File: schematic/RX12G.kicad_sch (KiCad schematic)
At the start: 11 parts, among them J1 ICSP, U1 PIC32MK1024GPK064-I/PT, X1 24 MHz

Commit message: Complete schematic
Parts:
- C1, C2, C3, C4, C5, C6, C7: footprint (none) -> Capacitor_SMD:C_0402_1005Metric
- J1: footprint (none) -> Connector_PinHeader_2.54mm:PinHeader_1x05_P2.54mm_Vertical
- R1: value R -> 10k; footprint (none) -> Resistor_SMD:R_0603_1608Metric
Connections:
- net CH9_SBUS4: now reaches U1.1 (TCK/RPA7/PMD5/RA7)
- net LED_SAT3: now reaches U1.11 (AN10/RPA12/RA12)
- net SAT3_RX: now reaches U1.12 (AN9/RPA11/RA11)
- net LED_SAT1: now reaches U1.14 (OA2IN+/AN1/C2IN1+/RPA1/RA1)
- net SAT1_RX: now reaches U1.15 (PGD3/VREF-/OA2IN-/AN2/C2IN1-/RPB0/CTED2/RB0)
- net Bind_Button: now reaches U1.16 (PGC3/OA1OUT/VREF+/AN3/C1IN4-/C4IN2-/RPB1/CTED1/PMA6/RB1)
- net LED_A: now reaches U1.21 (OA3OUT/AN6/C3IN4-/C4IN1+/C4IN4-/RPC0/RC0)
- net LED_B: now reaches U1.22 (OA3IN-/AN7/C3IN1-/C4IN1-/RPC1/PMA7/RC1)
- net IMU_INT2: now reaches U1.29 (AN14/RPE14/PMA1/RE14)
- net CH10_SBUS3: now reaches U1.3 (RPB15/PMD7/RB15)
- net IMU_INT1: now reaches U1.30 (AN15/RPE15/PMA0/RE15)
- net IMU_SDA: now reaches U1.31 (TDI/CDAC3/AN26/RPA8/SDA2/PMA9/RA8)
- net IMU_SCL: now reaches U1.32 (RPB4/SCL2/PMA8/RB4)
- net D-: now reaches U1.36 (D1-)
- net D+: now reaches U1.37 (D1+)
- net CH11_SBUS2: now reaches U1.4 (AN19/CVD19/RPG6/PMA5/RG6)
- net LED_SAT2: now reaches U1.42 (RD8)
- net SAT2_RX: now reaches U1.43 (PGD2/RPB5/SDA3/USBID1/RB5)
- net CH1: now reaches U1.49 (TMS/OA5IN-/AN27/CVD27/LVDIN/C5IN1-/RPB9/RB9)
- net CH2: now reaches U1.50 (TRCLK/RPC6/RC6)
- net CH3: now reaches U1.52 (TRD1/RPC8/PMWR/RC8)
- net CH4: now reaches U1.53 (TRD2/RPD5/PMRD/RD5)
- net CH5: now reaches U1.54 (TRD3/RPD6/RD6)
- net CH6: now reaches U1.55 (RPC9/RC9)
- net CH12_SBUS1: now reaches U1.6 (AN17/RPG8/SDA1/PMA3/RG8)
- net CH7: now reaches U1.62 (RPB12/PMD2/RB12)
- net CH8: now reaches U1.63 (RPB13/CTPLS/PMD3/RB13)
- no-connect marks 0 -> 20
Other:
- moved on the sheet: C1, C2, C3, C4, C5, C6, J1, R1

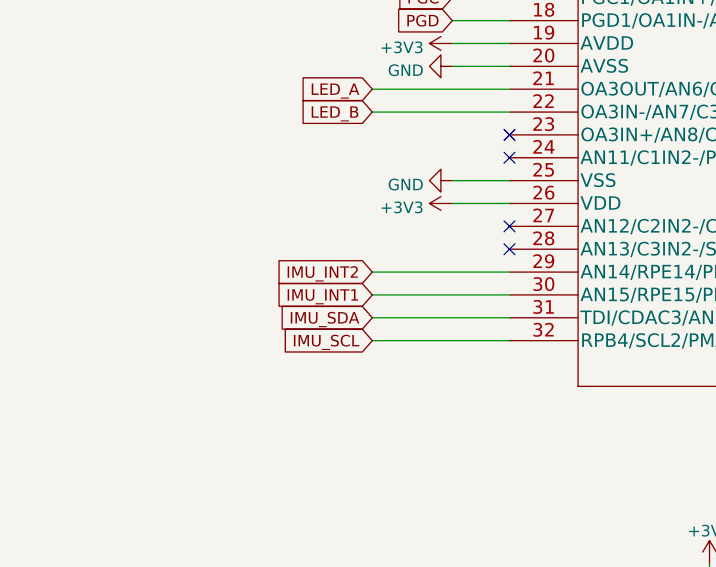
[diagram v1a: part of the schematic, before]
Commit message: Workable pcb layout
Needs work on silkscreen
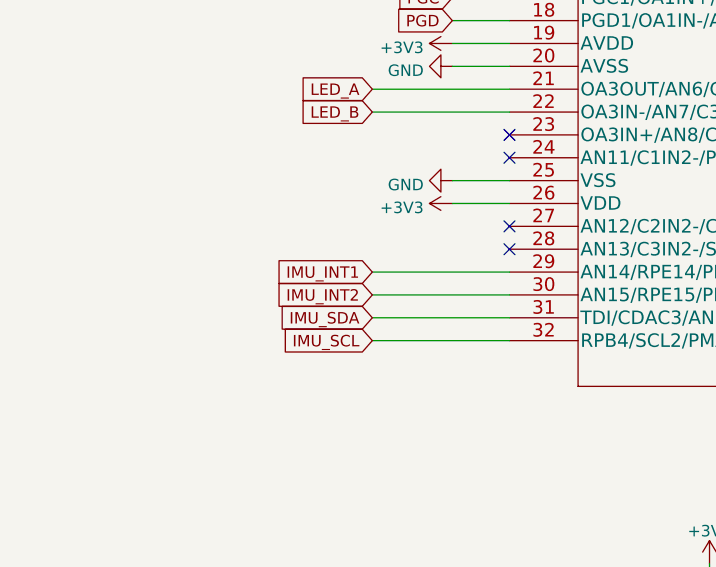
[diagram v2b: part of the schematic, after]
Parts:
- X1: footprint SamacSys Parts:AMPMAFB120000T -> SamacSys Parts:ASTMUPCE3312000MHZLJET
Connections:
- net IMU_INT1: now also U1.29 (AN14/RPE14/PMA1/RE14); no longer U1.30 (AN15/RPE15/PMA0/RE15)
- net IMU_INT2: now also U1.30 (AN15/RPE15/PMA0/RE15); no longer U1.29 (AN14/RPE14/PMA1/RE14)
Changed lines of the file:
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@@
+    (stroke (width 0) (type default) (color 0 0 0 0))
+  )
+  (wire (pts (xy 54.61 99.06) (xy 69.85 99.06))
     (stroke (width 0) (type default) (color 0 0 0 0))
   )
@@
     (stroke (width 0) (type default) (color 0 0 0 0))
   )
-  (wire (pts (xy 54.61 99.06) (xy 69.85 99.06))
-    (stroke (width 0) (type default) (color 0 0 0 0))
-  )
   (wire (pts (xy 92.075 131.445) (xy 92.075 135.255))
     (stroke (width 0) (type default) (color 0 0 0 0))
@@
     (stroke (width 0) (type default) (color 0 0 0 0))
   )
+  (wire (pts (xy 54.61 101.6) (xy 69.85 101.6))
+    (stroke (width 0) (type default) (color 0 0 0 0))
+  )
   (wire (pts (xy 130.175 142.875) (xy 142.875 142.875))
-    (stroke (width 0) (type default) (color 0 0 0 0))
-  )
-  (wire (pts (xy 54.61 101.6) (xy 69.85 101.6))
     (stroke (width 0) (type default) (color 0 0 0 0))
   )
@@
     )
   )
-  (global_label "IMU_INT1" (shape input) (at 54.61 101.6 180) (fields_autoplaced)
+  (global_label "IMU_INT1" (shape input) (at 54.61 99.06 180) (fields_autoplaced)
+    (effects (font (size 1.27 1.27)) (justify right))
+    (property "Intersheet References" "${INTERSHEET_REFS}" (id 0) (at 43.7302 98.9806 0)
+      (effects (font (size 1.27 1.27)) (justify right) hide)
+    )
+  )
+  (global_label "LED_A" (shape input) (at 54.61 78.74 180) (fields_autoplaced)
+    (effects (font (size 1.27 1.27)) (justify right))
+    (property "Intersheet References" "${INTERSHEET_REFS}" (id 0) (at 46.6936 78.6606 0)
+      (effects (font (size 1.27 1.27)) (justify right) hide)
+    )
+  )
+  (global_label "IMU_SCL" (shape input) (at 54.61 106.68 180) (fields_autoplaced)
+    (effects (font (size 1.27 1.27)) (justify right))
+    (property "Intersheet References" "${INTERSHEET_REFS}" (id 0) (at 44.335 106.6006 0)
+      (effects (font (size 1.27 1.27)) (justify right) hide)
+    )
+  )
+  (global_label "IMU_INT2" (shape input) (at 54.61 101.6 180) (fields_autoplaced)
     (effects (font (size 1.27 1.27)) (justify right))
     (property "Intersheet References" "${INTERSHEET_REFS}" (id 0) (at 43.7302 101.5206 0)
-      (effects (font (size 1.27 1.27)) (justify right) hide)
-    )
-  )
-  (global_label "LED_A" (shape input) (at 54.61 78.74 180) (fields_autoplaced)
-    (effects (font (size 1.27 1.27)) (justify right))
-    (property "Intersheet References" "${INTERSHEET_REFS}" (id 0) (at 46.6936 78.6606 0)
-      (effects (font (size 1.27 1.27)) (justify right) hide)
-    )
-  )
-  (global_label "IMU_SCL" (shape input) (at 54.61 106.68 180) (fields_autoplaced)
-    (effects (font (size 1.27 1.27)) (justify right))
-    (property "Intersheet References" "${INTERSHEET_REFS}" (id 0) (at 44.335 106.6006 0)
-      (effects (font (size 1.27 1.27)) (justify right) hide)
-    )
-  )
-  (global_label "IMU_INT2" (shape input) (at 54.61 99.06 180) (fields_autoplaced)
-    (effects (font (size 1.27 1.27)) (justify right))
-    (property "Intersheet References" "${INTERSHEET_REFS}" (id 0) (at 43.7302 98.9806 0)
       (effects (font (size 1.27 1.27)) (justify right) hide)
     )
@@
     (property "Reference" "X1" (id 0) (at 200.66 133.2443 0))
     (property "Value" "24 MHz" (id 1) (at 200.66 136.0194 0))
-    (property "Footprint" "SamacSys Parts:AMPMAFB120000T" (id 2) (at 212.09 137.16 0)
+    (property "Footprint" "SamacSys Parts:ASTMUPCE3312000MHZLJET" (id 2) (at 212.09 137.16 0)
       (effects (font (size 1.27 1.27)) (justify left) hide)
     )
@@
     )
     (path "/fb9fbb52-14d4-4062-9475-ec74defe9327"
-      (reference "X1") (unit 1) (value "24 MHz") (footprint "SamacSys Parts:AMPMAFB120000T")
-    )
-  )
+      (reference "X1") (unit 1) (value "24 MHz") (footprint "SamacSys Parts:ASTMUPCE3312000MHZLJET")
+    )
+  )

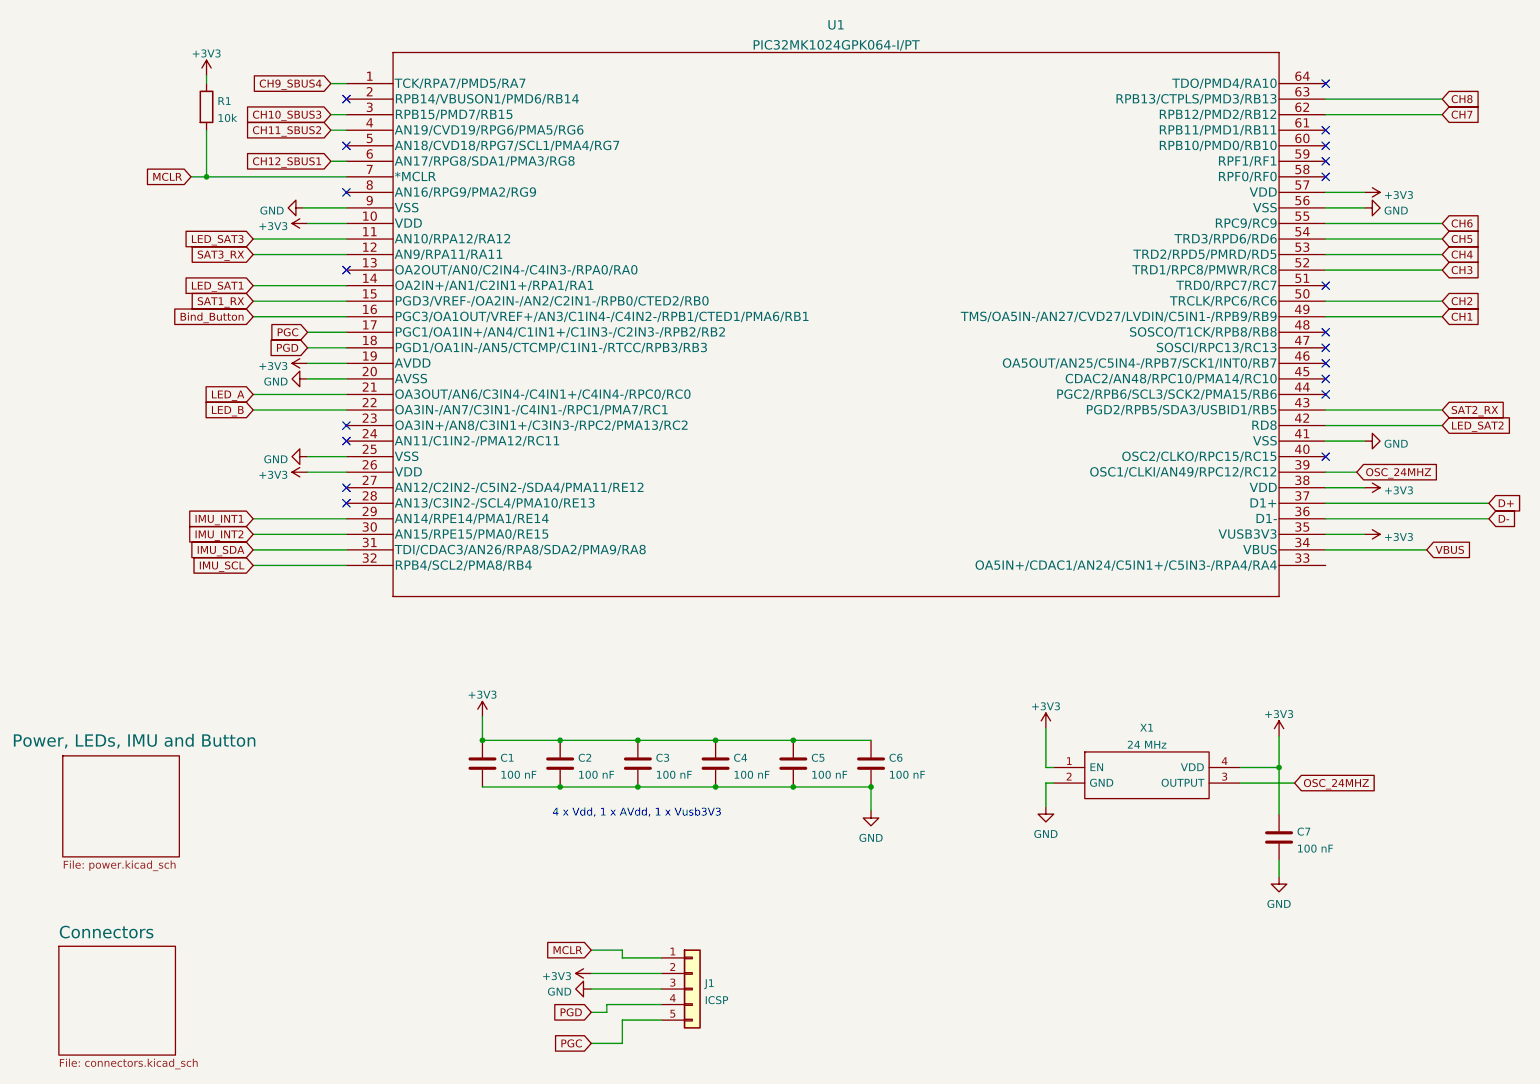
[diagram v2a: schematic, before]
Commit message: Fixed missing  SAT_POWER connection
Also re-assigned some pins to improve pcb layout
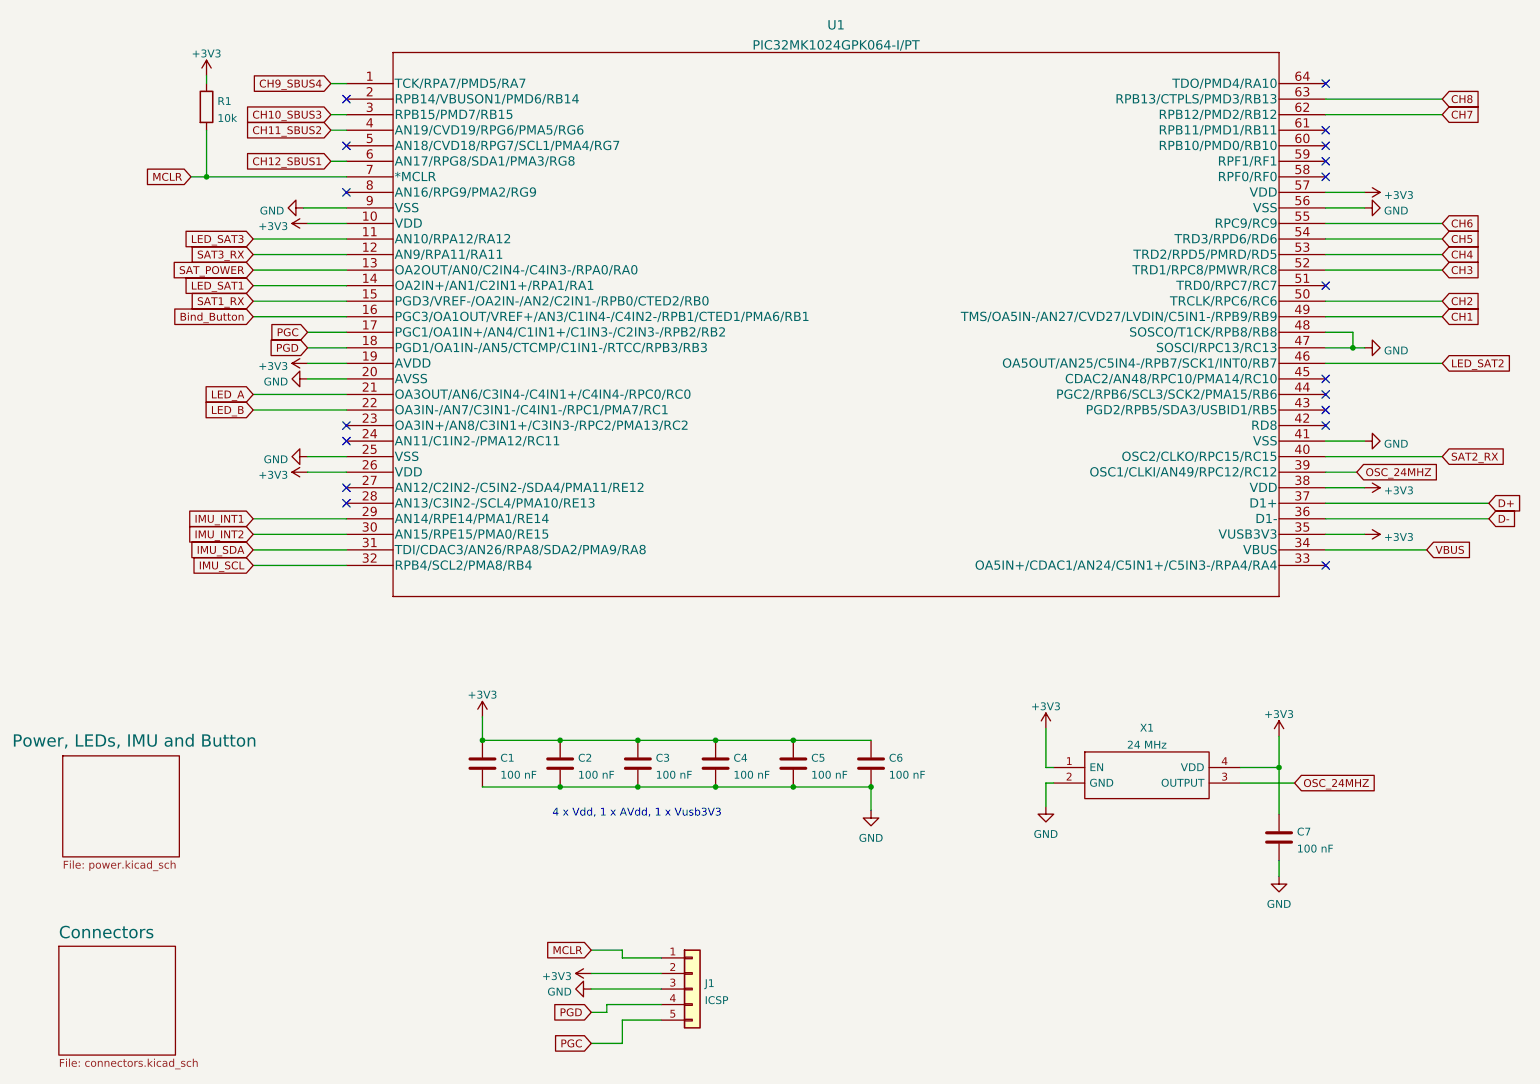
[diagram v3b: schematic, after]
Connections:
- net GND: now also U1.47 (SOSCI/RPC13/RC13), U1.48 (SOSCO/T1CK/RPB8/RB8)
- net LED_SAT2: now also U1.46 (OA5OUT/AN25/C5IN4-/RPB7/SCK1/INT0/RB7); no longer U1.42 (RD8)
- net SAT2_RX: now also U1.40 (OSC2/CLKO/RPC15/RC15); no longer U1.43 (PGD2/RPB5/SDA3/USBID1/RB5)
- net SAT_POWER: now reaches U1.13 (OA2OUT/AN0/C2IN4-/C4IN3-/RPA0/RA0)
- no-connect marks 20 -> 18
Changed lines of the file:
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@@
   (junction (at 142.875 142.875) (diameter 0) (color 0 0 0 0)
   )
+  (junction (at 234.315 71.12) (diameter 0) (color 0 0 0 0)
+  )
   (junction (at 46.99 43.18) (diameter 0) (color 0 0 0 0)
   )
@@
   (junction (at 117.475 135.255) (diameter 0) (color 0 0 0 0)
   )
-  (no_connect (at 69.85 58.42))
   (no_connect (at 69.85 83.82))
   (no_connect (at 69.85 86.36))
@@
   (no_connect (at 69.85 93.98))
   (no_connect (at 69.85 45.72))
+  (no_connect (at 229.87 106.68))
   (no_connect (at 69.85 30.48))
   (no_connect (at 69.85 38.1))
@@
   (no_connect (at 229.87 38.1))
   (no_connect (at 229.87 35.56))
-  (no_connect (at 229.87 88.9))
   (no_connect (at 229.87 78.74))
   (no_connect (at 229.87 43.18))
-  (no_connect (at 229.87 68.58))
-  (no_connect (at 229.87 71.12))
-  (no_connect (at 229.87 73.66))
   (no_connect (at 229.87 76.2))
   (no_connect (at 229.87 60.96))
+  (no_connect (at 229.87 81.28))
+  (no_connect (at 229.87 83.82))
   (wire (pts (xy 114.935 170.815) (xy 121.285 170.815))
     (stroke (width 0) (type default) (color 0 0 0 0))
@@
     (stroke (width 0) (type default) (color 0 0 0 0))
   )
+  (wire (pts (xy 234.315 68.58) (xy 234.315 71.12))
+    (stroke (width 0) (type default) (color 0 0 0 0))
+  )
   (wire (pts (xy 229.87 91.44) (xy 234.95 91.44))
     (stroke (width 0) (type default) (color 0 0 0 0))
@@
     (stroke (width 0) (type default) (color 0 0 0 0))
   )
+  (wire (pts (xy 54.61 58.42) (xy 69.85 58.42))
+    (stroke (width 0) (type default) (color 0 0 0 0))
+  )
   (wire (pts (xy 229.87 104.14) (xy 246.38 104.14))
     (stroke (width 0) (type default) (color 0 0 0 0))
@@
     (stroke (width 0) (type default) (color 0 0 0 0))
   )
+  (wire (pts (xy 229.87 88.9) (xy 248.92 88.9))
+    (stroke (width 0) (type default) (color 0 0 0 0))
+  )
   (wire (pts (xy 142.875 135.255) (xy 155.575 135.255))
     (stroke (width 0) (type default) (color 0 0 0 0))
@@
     (stroke (width 0) (type default) (color 0 0 0 0))
   )
-  (wire (pts (xy 229.87 83.82) (xy 248.92 83.82))
-    (stroke (width 0) (type default) (color 0 0 0 0))
-  )
   (wire (pts (xy 46.99 43.18) (xy 69.85 43.18))
     (stroke (width 0) (type default) (color 0 0 0 0))
@@
     (stroke (width 0) (type default) (color 0 0 0 0))
   )
-  (wire (pts (xy 229.87 81.28) (xy 248.92 81.28))
-    (stroke (width 0) (type default) (color 0 0 0 0))
-  )
   (wire (pts (xy 222.25 139.7) (xy 222.25 147.32))
     (stroke (width 0) (type default) (color 0 0 0 0))
@@
     (stroke (width 0) (type default) (color 0 0 0 0))
   )
+  (wire (pts (xy 229.87 71.12) (xy 234.315 71.12))
+    (stroke (width 0) (type default) (color 0 0 0 0))
+  )
   (wire (pts (xy 222.25 154.94) (xy 222.25 157.48))
     (stroke (width 0) (type default) (color 0 0 0 0))
@@
     (stroke (width 0) (type default) (color 0 0 0 0))
   )
+  (wire (pts (xy 229.87 68.58) (xy 234.315 68.58))
+    (stroke (width 0) (type default) (color 0 0 0 0))
+  )
   (wire (pts (xy 46.99 26.67) (xy 46.99 27.94))
     (stroke (width 0) (type default) (color 0 0 0 0))
@@
     (stroke (width 0) (type default) (color 0 0 0 0))
   )
+  (wire (pts (xy 229.87 73.66) (xy 248.92 73.66))
+    (stroke (width 0) (type default) (color 0 0 0 0))
+  )
   (wire (pts (xy 130.175 142.875) (xy 142.875 142.875))
     (stroke (width 0) (type default) (color 0 0 0 0))
@@
   )
   (wire (pts (xy 109.855 173.355) (xy 121.285 173.355))
+    (stroke (width 0) (type default) (color 0 0 0 0))
+  )
+  (wire (pts (xy 234.315 71.12) (xy 236.22 71.12))
     (stroke (width 0) (type default) (color 0 0 0 0))
   )
@@
     )
   )
-  (global_label "SAT2_RX" (shape input) (at 248.92 81.28 0) (fields_autoplaced)
-    (effects (font (size 1.27 1.27)) (justify left))
-    (property "Intersheet References" "${INTERSHEET_REFS}" (id 0) (at 259.2555 81.2006 0)
+  (global_label "SAT2_RX" (shape input) (at 248.92 88.9 0) (fields_autoplaced)
+    (effects (font (size 1.27 1.27)) (justify left))
+    (property "Intersheet References" "${INTERSHEET_REFS}" (id 0) (at 259.2555 88.8206 0)
       (effects (font (size 1.27 1.27)) (justify left) hide)
     )
@@
     )
   )
+  (global_label "SAT_POWER" (shape input) (at 54.61 58.42 180) (fields_autoplaced)
+    (effects (font (size 1.27 1.27)) (justify right))
+    (property "Intersheet References" "${INTERSHEET_REFS}" (id 0) (at 41.4926 58.3406 0)
+      (effects (font (size 1.27 1.27)) (justify right) hide)
+    )
+  )
   (global_label "LED_SAT3" (shape input) (at 54.61 53.34 180) (fields_autoplaced)
     (effects (font (size 1.27 1.27)) (justify right))
@@
     )
   )
-  (global_label "LED_SAT2" (shape input) (at 248.92 83.82 0) (fields_autoplaced)
-    (effects (font (size 1.27 1.27)) (justify left))
-    (property "Intersheet References" "${INTERSHEET_REFS}" (id 0) (at 260.2231 83.7406 0)
+  (global_label "LED_SAT2" (shape input) (at 248.92 73.66 0) (fields_autoplaced)
+    (effects (font (size 1.27 1.27)) (justify left))
+    (property "Intersheet References" "${INTERSHEET_REFS}" (id 0) (at 260.2231 73.5806 0)
       (effects (font (size 1.27 1.27)) (justify left) hide)
     )
@@
     )
     (property "Datasheet" "" (id 3) (at 184.15 146.05 0)
+      (effects (font (size 1.27 1.27)) hide)
+    )
+    (pin "1")
+  )
+  (symbol (lib_id "power:GND") (at 236.22 71.12 90) (unit 1)
+    (in_bom yes) (on_board yes) (fields_autoplaced)
+    (property "Reference" "#PWR0134" (id 0) (at 242.57 71.12 0)
+      (effects (font (size 1.27 1.27)) hide)
+    )
+    (property "Value" "GND" (id 1) (at 239.395 71.599 90)
+      (effects (font (size 1.27 1.27)) (justify right))
+    )
+    (property "Footprint" "" (id 2) (at 236.22 71.12 0)
+      (effects (font (size 1.27 1.27)) hide)
+    )
+    (property "Datasheet" "" (id 3) (at 236.22 71.12 0)
       (effects (font (size 1.27 1.27)) hide)
     )
@@
       (reference "#PWR0133") (unit 1) (value "+3V3") (footprint "")
     )
+    (path "/912c0221-f944-46f6-ba12-3bff265e898a"
+      (reference "#PWR0134") (unit 1) (value "GND") (footprint "")
+    )
     (path "/4c99303f-ffc1-4ad9-aa26-af99f179c5f3"

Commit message: Update to KiCad 9.0
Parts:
- U1: symbol PIC32MK:PIC32MK1024GPK064-I/PT -> PIC32MK:PIC32MK1024GPK064-I/PT
